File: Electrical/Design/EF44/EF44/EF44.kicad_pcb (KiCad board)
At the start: 4 copper layers, 100 x 100 mm, 154 parts, among them J1 USB_C_TYPE-C-32-M-12, J10 Conn_01x08, J11 Conn_01x08, J2 N.F., J4 Conn_01x08, J5 Conn_01x08, J6 Conn_01x08, J7 Conn_01x08, J8 Conn_01x08, J9 Conn_01x08, M1 Conn_01x08, SW1 SW_SPST, U1 74HC165, U10 74HC4051, U15 FUSB302BMPX, U16 FUSB302BMPX(N.F.), U17 MT9700, U2 74HC165, U3 74HC165, U4 SESRV05-4, U5 LN1134A332MR-G, U6 LN1134A332MR-G, U7 SAMD51N20A, U8 W25Q16JVSSIQ, U9 74HC4051

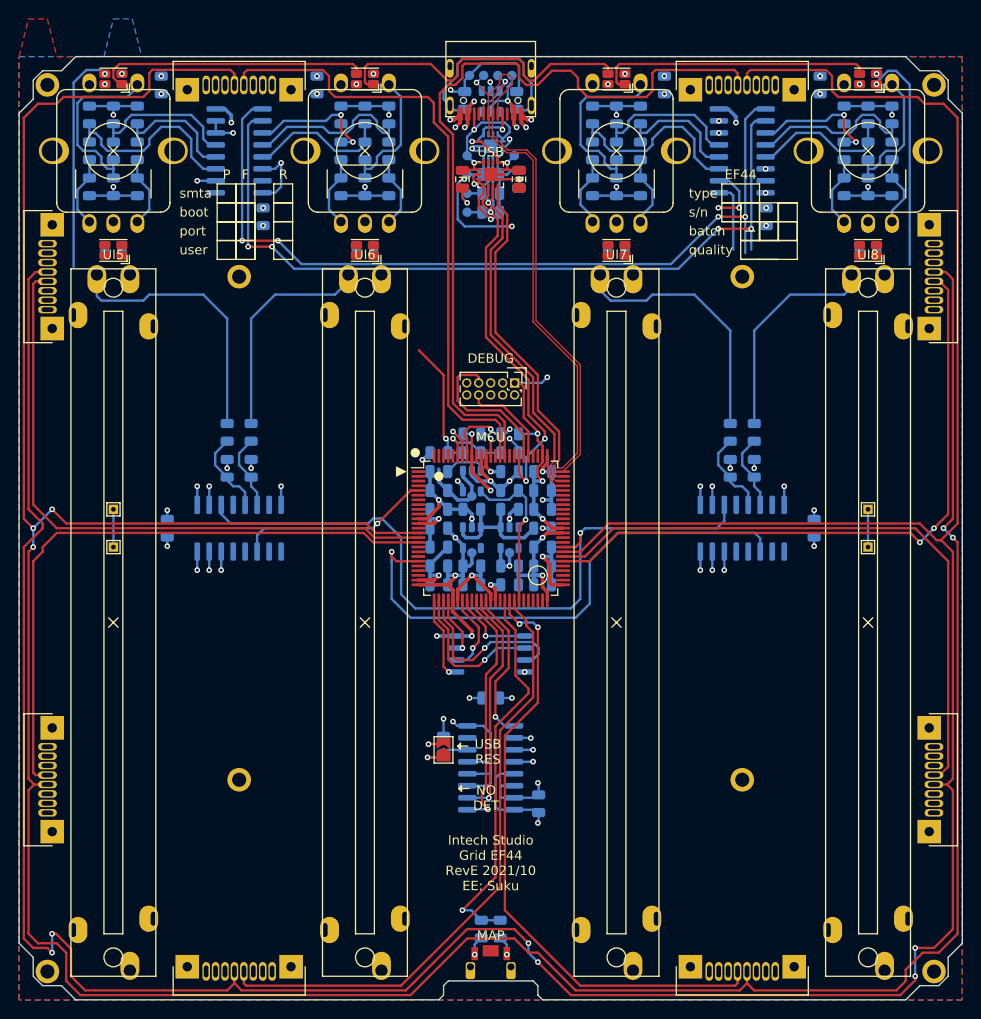
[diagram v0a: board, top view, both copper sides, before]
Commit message: SUKU EF44 and YAML reverted to stable kicad
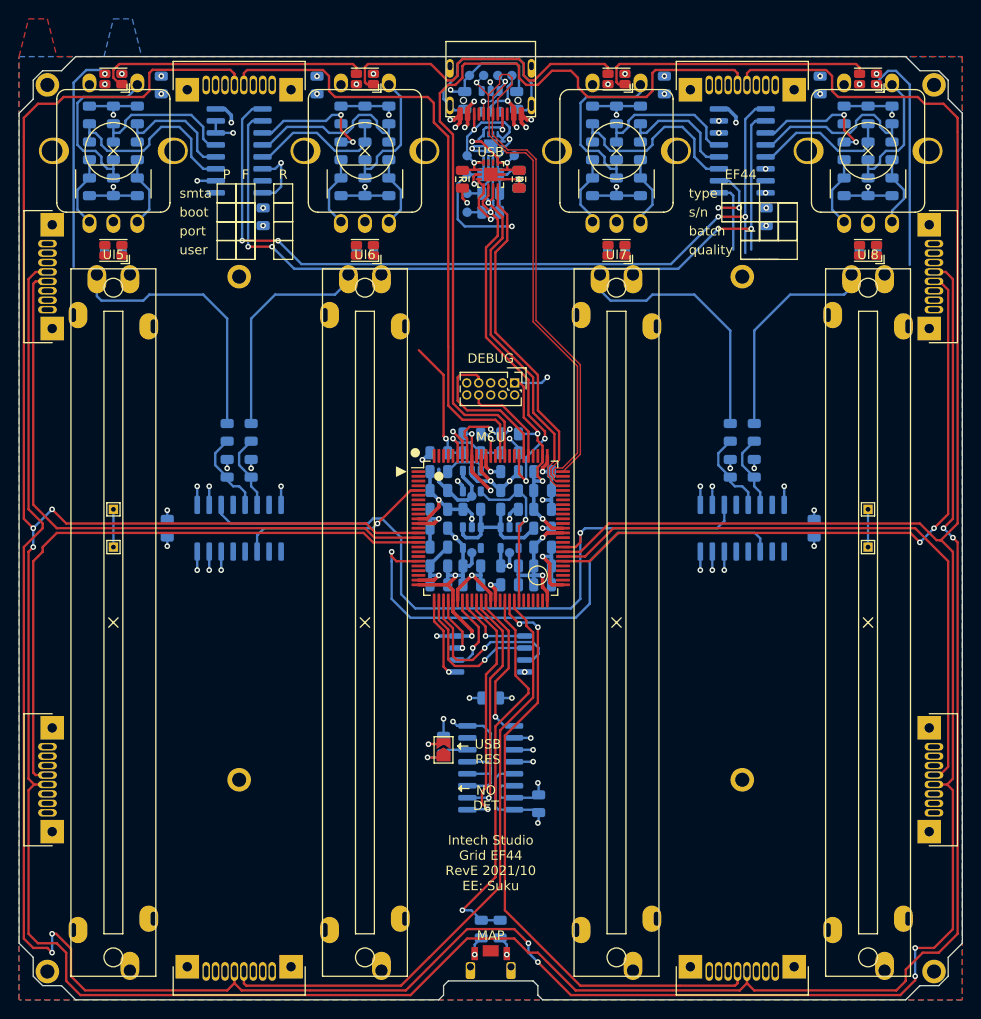
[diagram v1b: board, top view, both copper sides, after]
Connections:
- net /MCU/QSPI_~{CE} renamed /MCU/QSPI_~CE
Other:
- net class Default added: clearance 0.1, trace_width 0.254, via_dia 0.6, via_drill 0.3
- net class USB2.0 added: clearance 0.1524, trace_width 0.1524, via_dia 0.6, via_drill 0.3

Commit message: SUKU EF44 DRC and YAML tuned
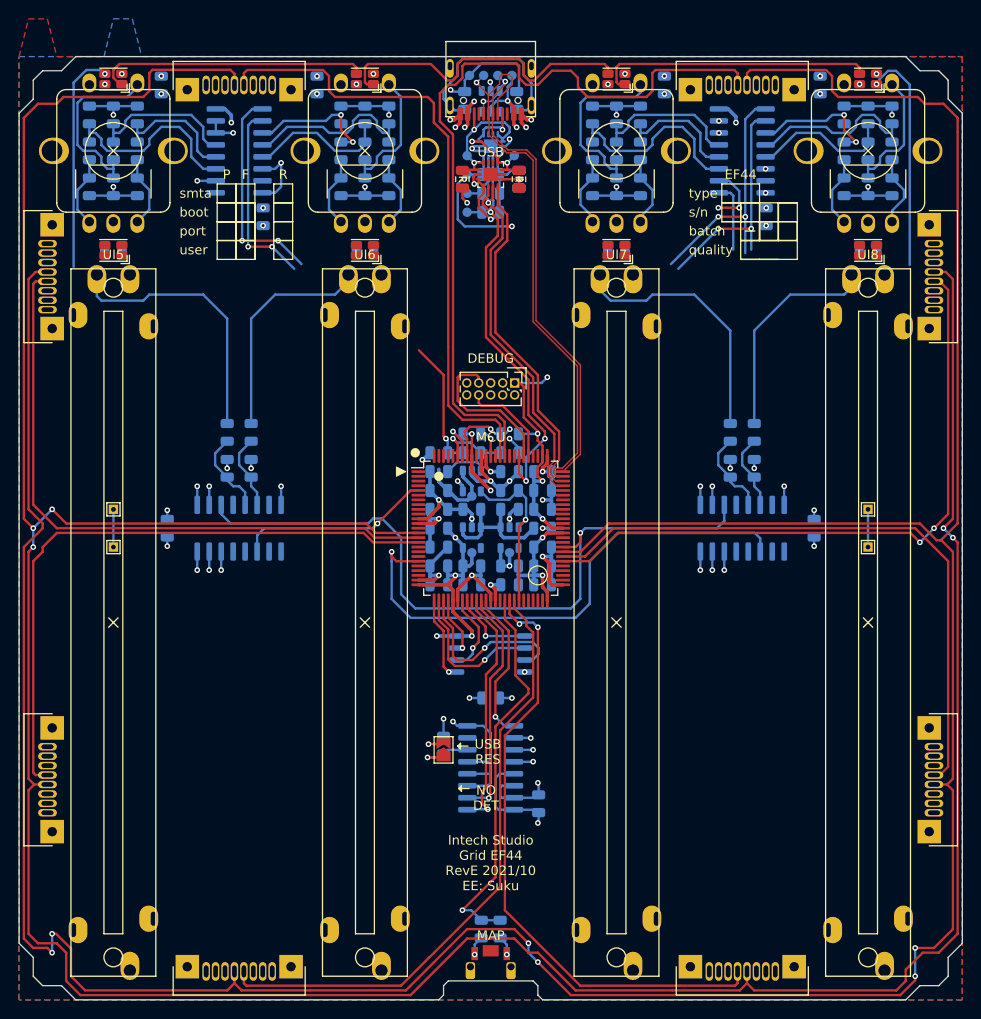
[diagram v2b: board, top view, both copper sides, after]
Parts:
- removed M1: Conn_01x08, suku_basics:grid_outline
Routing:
- net /UI_ENC/ENCODER_SCK: track 85.6 -> 44.9 mm
- net /UI_ENC/ENCODER_CS: track 88.7 -> 49.6 mm

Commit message: SUKU EF44 build automation fixed for position files
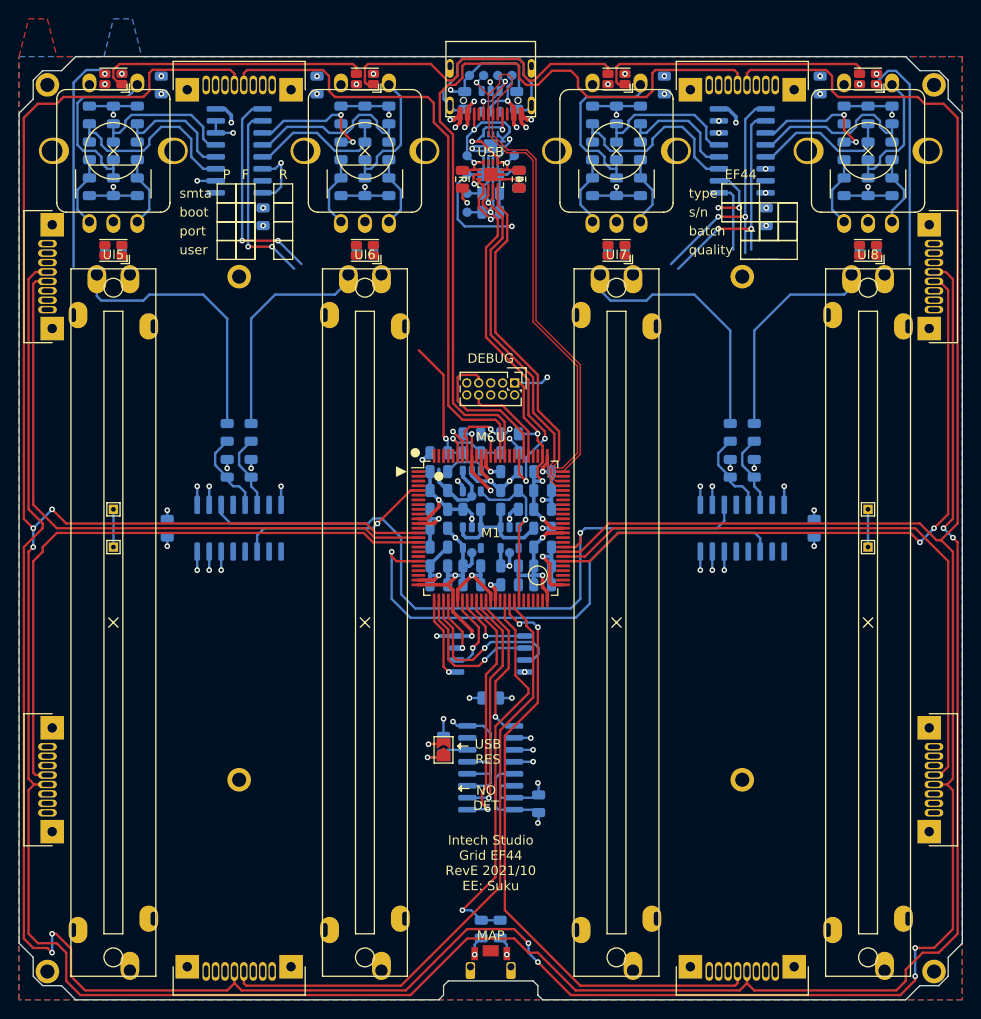
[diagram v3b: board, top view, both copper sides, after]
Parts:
- added M1: Conn_01x08, suku_basics:grid_outline, F.Cu at (100.0, 100.0)
- U1, U2, U3: footprint suku_basics:SOIC-16_3.9x9.9mm_P1.27mm(rot90) -> suku_basics:SOIC-16_74HC165
- U10, U9: footprint suku_basics:SOIC-16_3.9x9.9mm_P1.27mm -> suku_basics:SOIC-16_74HC4051
- U8: footprint suku_basics:SOIC-8_WIDE(rot90) -> suku_basics:SOIC-8W_FLASH
- turned U1 to 180 degrees
- turned U2 to 180 degrees
- turned U3 to 0 degrees
- turned U8 to 180 degrees

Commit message: SUKU EF44 pcb designed
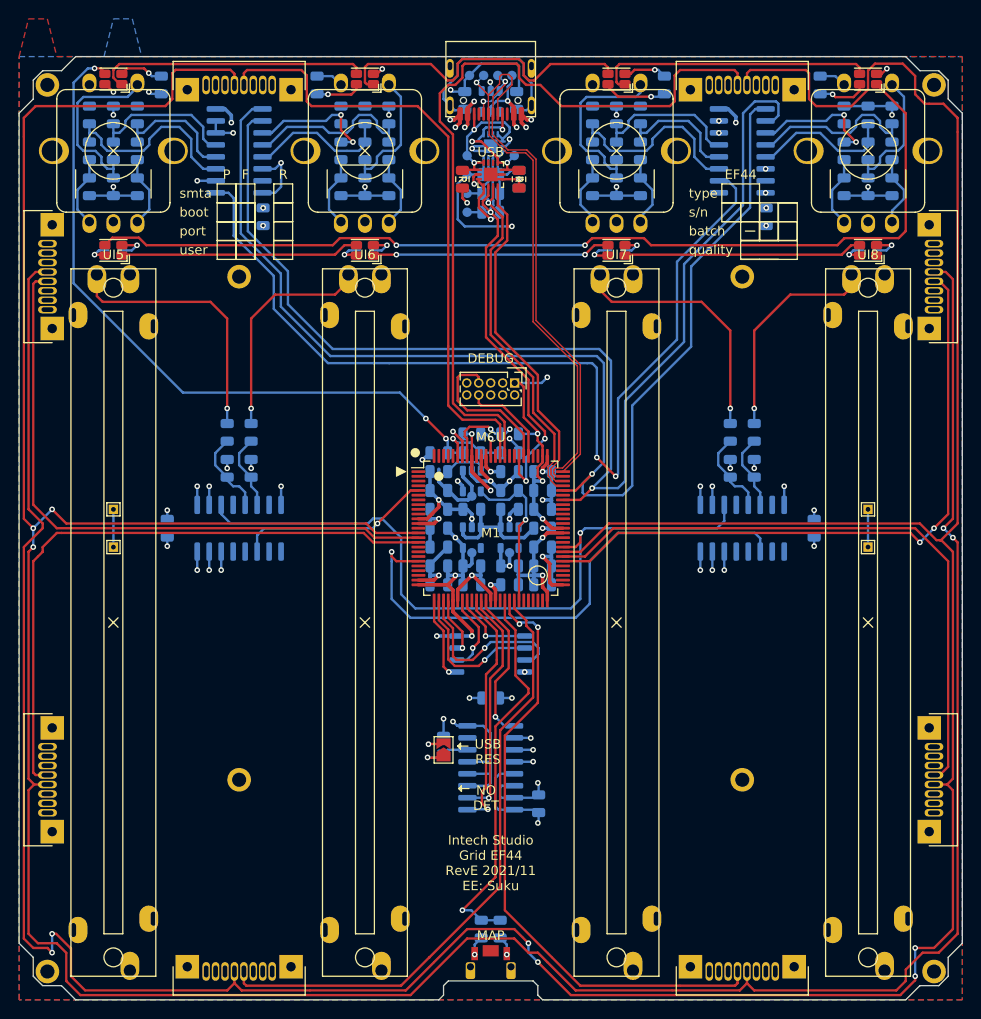
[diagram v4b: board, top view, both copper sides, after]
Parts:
- turned C1 to 270 degrees
- turned C2 to 270 degrees
- turned C3 to 270 degrees
- turned C4 to 270 degrees
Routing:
- net Net-(U1-Pad9): track 6.60 -> 102.7 mm
- net /UI_ENC/ENCODER_SCK: track 44.9 -> 132.3 mm, vias 4 -> 1
- net /UI_ENC/ENCODER_CS: track 49.6 -> 131.7 mm, vias 4 -> 1
- net Net-(D4-Pad1): track 24.1 -> 104.3 mm, vias 1 -> 2
- net /UI_LED/LED_DATA_IN: track 37.5 -> 75.1 mm, vias 2 -> 3
- net +5V_UI: track 8.87 -> 39.2 mm, vias 8 -> 9
- net GND: track 197.3 -> 227.5 mm
- net Net-(D6-Pad1): track 0.00 -> 25.3 mm, vias 0 -> 2
- net Net-(D5-Pad1): track 0.00 -> 25.3 mm
- net Net-(D7-Pad1): track 0.00 -> 25.3 mm
- net Net-(U2-Pad9): track 7.37 -> 0.00 mm
- net /MCU/GRID_SYNC_1: track 350.0 -> 356.7 mm
- net /MCU/GRID_NORTH_TX: track 84.7 -> 84.1 mm
- net Net-(R26-Pad2): track 27.6 -> 27.1 mm, vias 0 -> 1
- net Net-(R25-Pad2): track 28.7 -> 28.2 mm, vias 0 -> 1
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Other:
- board text added: "Intech Studio Grid EF44 RevE 2021/11 EE: Suku"
- board text removed: "Intech Studio Grid EF44 RevE 2021/10 EE: Suku"

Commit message: SUKU EF44 footprints updated
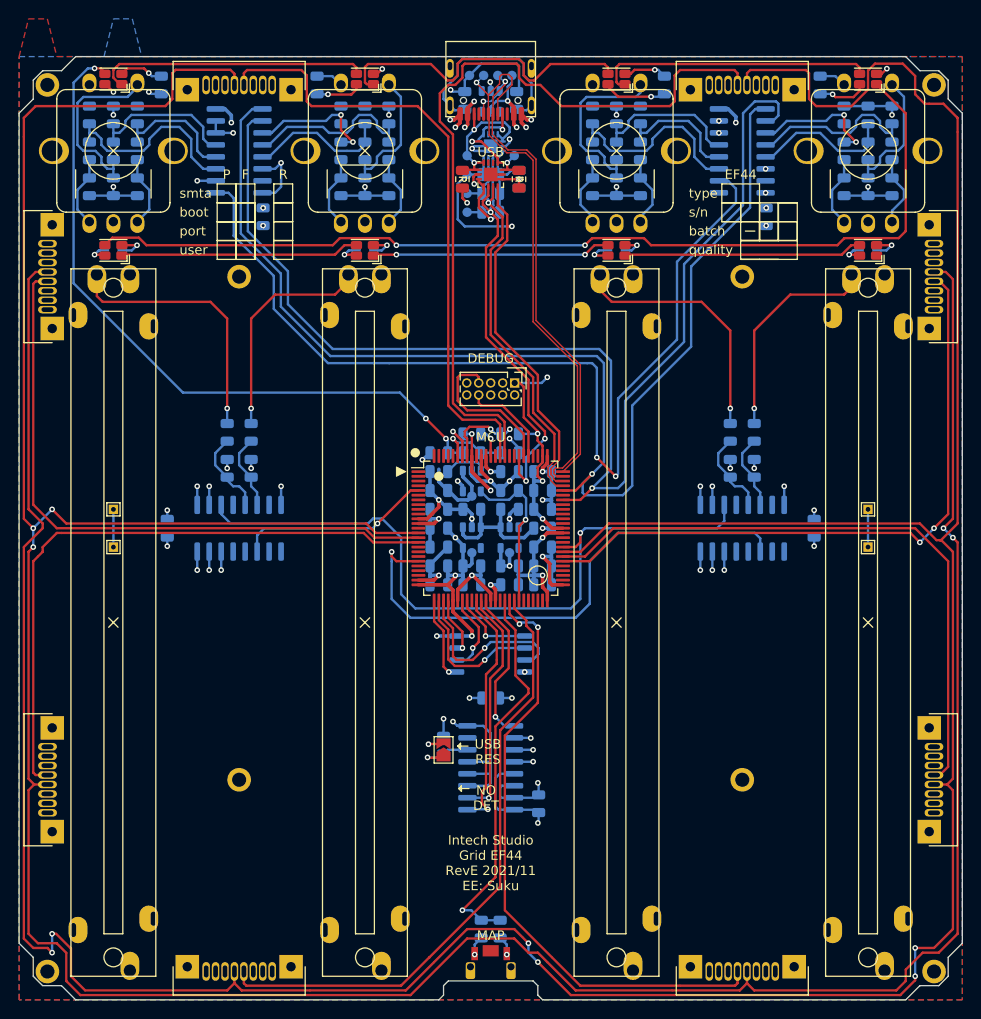
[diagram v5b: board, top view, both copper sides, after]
